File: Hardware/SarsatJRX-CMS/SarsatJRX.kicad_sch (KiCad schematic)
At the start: 37 parts, among them J3 LilyPi GPIO Header, U1 TLC2274, U2 TLC2274

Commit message: Added schematics.
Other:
- company: (none) -> F4JRX - ADRASEC 31
- title: (none) -> SarsatJRX signal board
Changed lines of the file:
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@@
 	(generator_version "9.0")
 	(paper "A4")
+	(title_block
+		(title "SarsatJRX signal board")
+		(date "2025-05-23")
+		(rev "v1.0")
+		(company "F4JRX - ADRASEC 31")
+		(comment 1 "Based on the work of Jean-Paul YONNET (F1LVT) : https://f1lvt.com/")
+		(comment 2 "SIgnal board for SarsatJRX decoder by F4JRX")
+	)
 	(junction
 		(at 262.89 43.18)

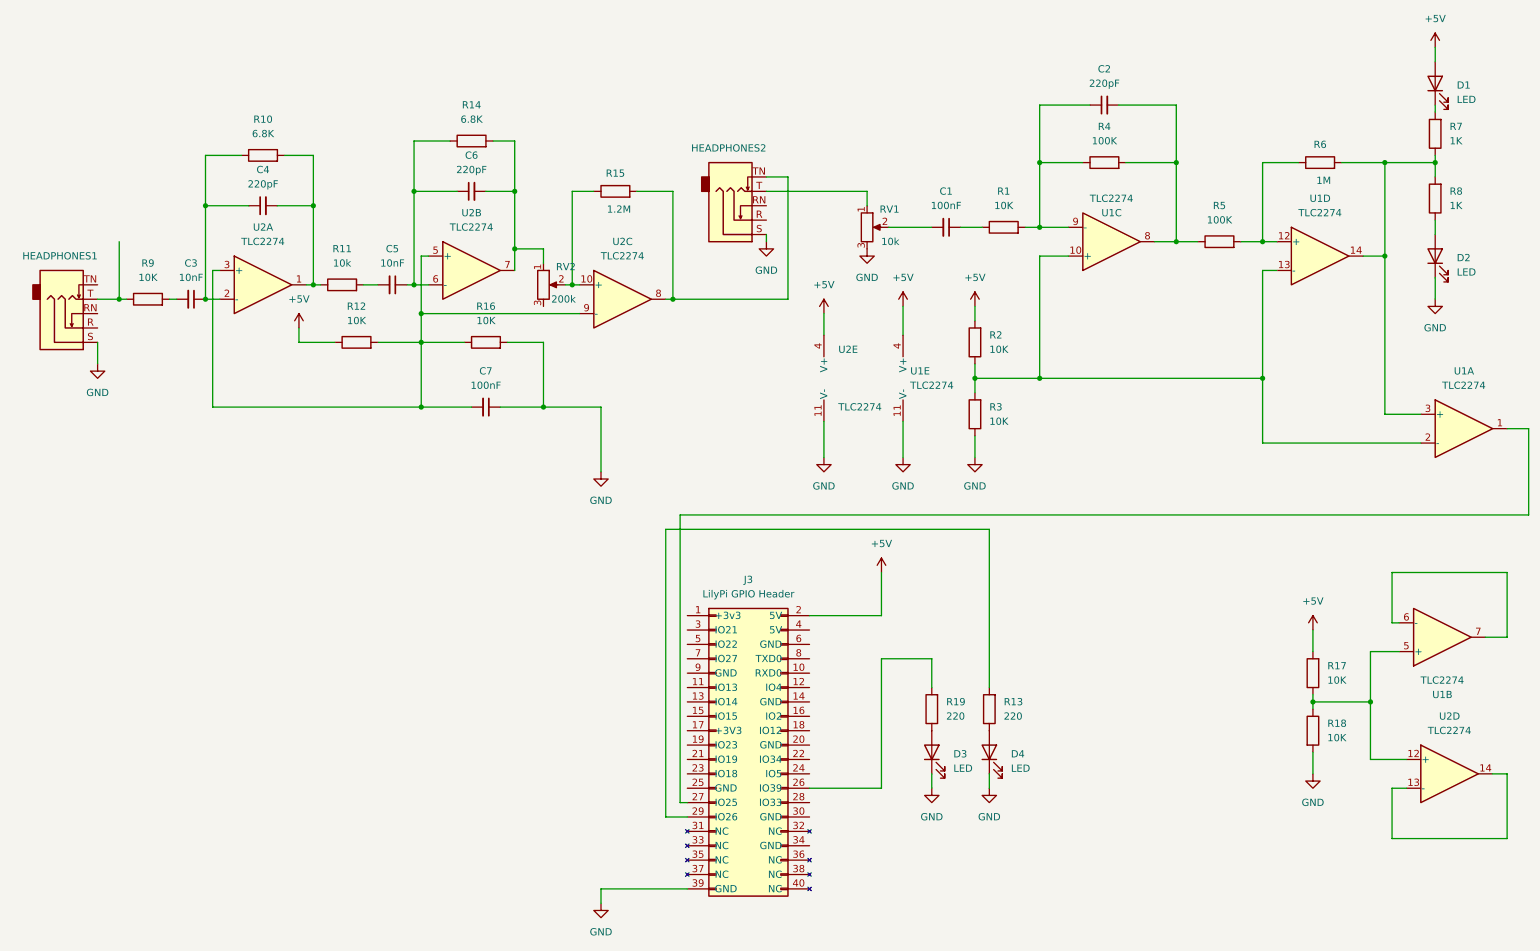
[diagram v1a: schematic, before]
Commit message: First step to v1.1 of the board : - Added buzzer on IO33 - Mouved led err to IO04 - Added voltage adaptation (5v->3.3v) on Receiver pin (IO25) - Added discri jack insertion detection on IO39 - Added audio input on IO34 - Added decoupling capacitors on 5V power supply for U1 and U2 to try and prevent spikes when wifi is activated - Added ground plane on bottom side of the PCB
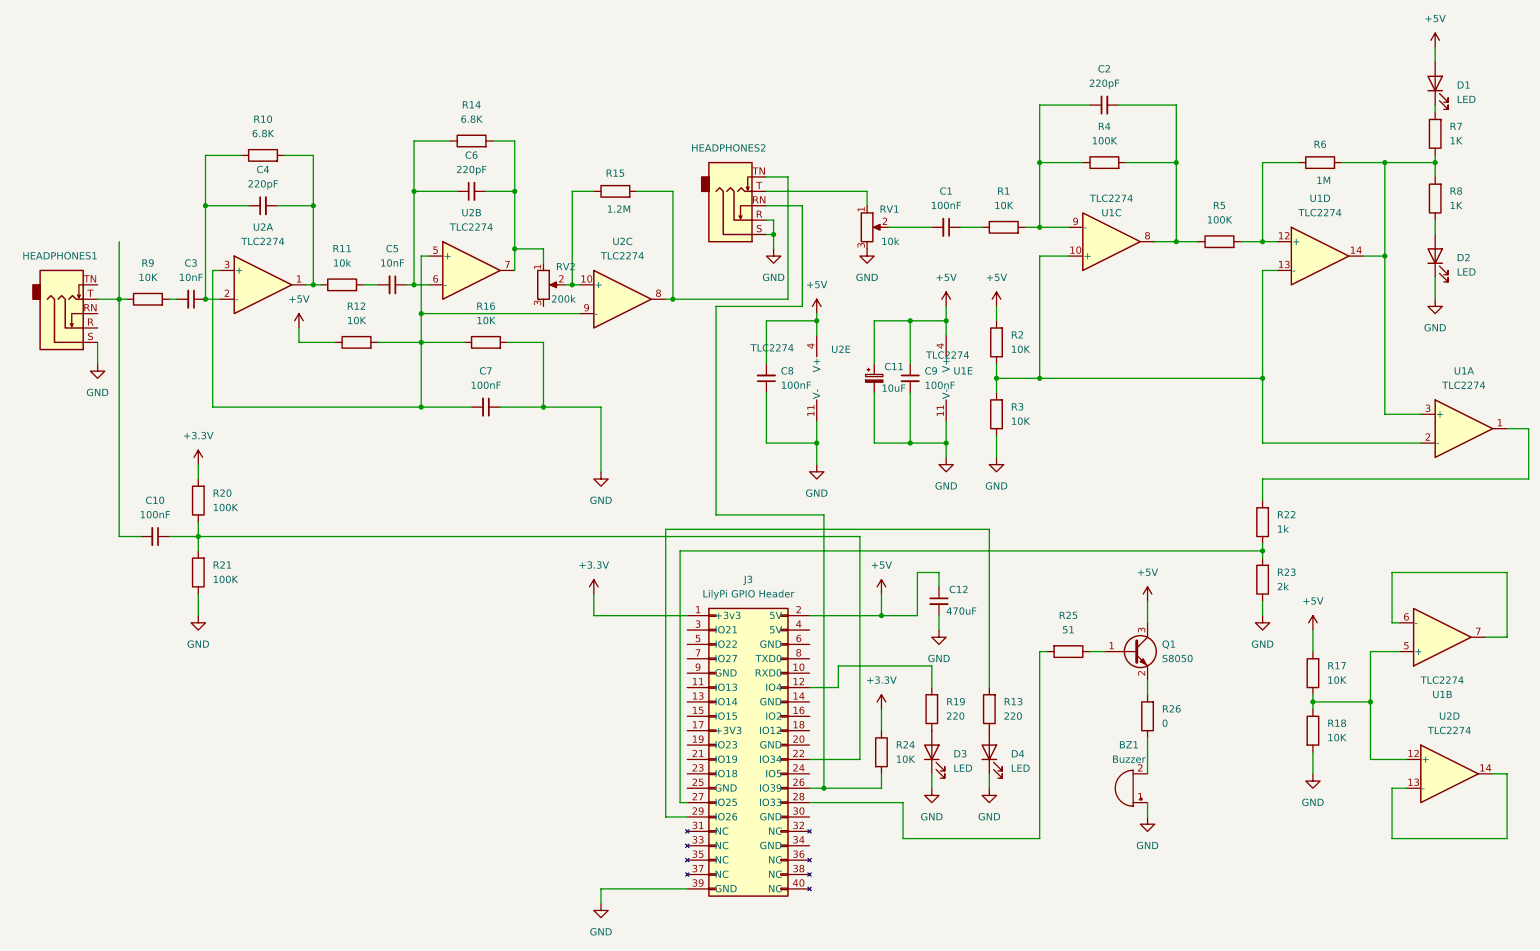
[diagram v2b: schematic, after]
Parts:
- added BZ1: Buzzer, Buzzer:MagneticBuzzer_PUI_AT-0927-TT-6-R-side-horn, symbol Device:Buzzer
- added C10, C8, C9: 100nF, Capacitor_SMD:C_0603_1608Metric, symbol Device:C_Small
- added C11: 10uF, Capacitor_Tantalum_SMD:CP_EIA-3216-18_Kemet-A, symbol Device:C_Polarized_Small
- added C12: 470uF, Capacitor_THT:CP_Radial_D8.0mm_P3.50mm, symbol Device:C_Small
- added Q1: S8050, j3y:SOT-23-3_L3.0-W1.7-P0.95-LS2.9-BR, symbol Transistor_BJT:S8050
- added R20, R21: 100K, Resistor_SMD:R_0603_1608Metric, symbol Device:R
- added R22: 1k, Resistor_SMD:R_0603_1608Metric, symbol Device:R
- added R23: 2k, Resistor_SMD:R_0603_1608Metric, symbol Device:R
- added R24: 10K, Resistor_SMD:R_0603_1608Metric, symbol Device:R
- added R25: 51, Resistor_SMD:R_0603_1608Metric, symbol Device:R
- added R26: 0, Resistor_SMD:R_0603_1608Metric, symbol Device:R
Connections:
- net +5V: now also C11.1, C12.1, C8.2, C9.1, Q1.3 (C)
- net GND: now also HEADPHONES2.R, BZ1.1 (+), C11.2, C12.2, C8.1, C9.2, R21.1, R23.1
- net +3.3V: now reaches J3.1 (+3v3)
- net +3.3V: now also R20.2, R24.1
- net at J3.12 (IO4): now also R19.2
- net at J3.22 (IO34): now also C10.1, R20.1, R21.2
- net at J3.26 (IO39): now also HEADPHONES2.RN, R24.2; no longer R19.2
- net at J3.27 (IO25): now also R22.1, R23.2; no longer U1.1
- net at J3.28 (IO33): now also R25.2
- net at HEADPHONES1.T, R9.1: now also C10.2
- new net: BZ1.2 (-), R26.1
- new net: Q1.2 (E), R26.2
- new net: Q1.1 (B), R25.1
- new net: R22.2, U1.1
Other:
- moved on the sheet: R2, R3, U1E, U2E

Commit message: Added test points.
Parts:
- added TP1, TP2, TP3, TP4, TP5, TP6: ~, TestPoint:TestPoint_Pad_D1.0mm, symbol Connector:TestPoint
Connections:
- net at C3.1, C4.1, R10.1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: now also TP6.1
- net at C10.2, HEADPHONES1.T, R9.1: now also TP3.1
- net at J3.27 (IO25), R22.1, R23.2: now also TP2.1
- net at R22.2, U1.1: now also TP1.1
- net at C2.1, R1.2, R4.1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: now also TP5.1
- net at HEADPHONES2.T, RV1.1: now also TP4.1

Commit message: Fixed more silk screen. Added 2 test points.
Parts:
- added TP7, TP8: ~, TestPoint:TestPoint_Pad_D1.0mm, symbol Connector:TestPoint
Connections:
- net at HEADPHONES2.RN, J3.26 (IO39), R24.2: now also TP8.1
- net at C10.1, J3.22 (IO34), R20.1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: now also TP7.1
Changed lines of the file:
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@@
 	)
 	(junction
+		(at 142.24 105.41)
+		(diameter 0)
+		(color 0 0 0 0)
+	)
+	(junction
 		(at 110.49 64.77)
 		(diameter 0)
@@
 	)
 	(junction
+		(at 78.74 109.22)
+		(diameter 0)
+		(color 0 0 0 0)
+	)
+	(junction
 		(at 232.41 111.76)
 		(diameter 0)
@@
 	(wire
 		(pts
-			(xy 44.45 109.22) (xy 161.29 109.22)
+			(xy 44.45 109.22) (xy 78.74 109.22)
 		)
 		(stroke
@@
 	(wire
 		(pts
+			(xy 78.74 109.22) (xy 161.29 109.22)
+		)
+		(stroke
+			(width 0)
+			(type default)
+		)
+	)
+	(wire
+		(pts
 			(xy 176.53 88.9) (xy 176.53 92.71)
 		)
@@
 	(wire
 		(pts
-			(xy 135.89 105.41) (xy 154.94 105.41)
+			(xy 135.89 105.41) (xy 142.24 105.41)
 		)
 		(stroke
@@
 	(wire
 		(pts
+			(xy 142.24 105.41) (xy 154.94 105.41)
+		)
+		(stroke
+			(width 0)
+			(type default)
+		)
+	)
+	(wire
+		(pts
 			(xy 163.83 71.12) (xy 170.18 71.12)
 		)
@@
 	)
 	(symbol
+		(lib_id "Connector:TestPoint")
+		(at 142.24 105.41 0)
+		(unit 1)
+		(exclude_from_sim no)
+		(in_bom yes)
+		(on_board yes)
+		(dnp no)
+		(property "Reference" "TP8"
+			(at 141.224 100.33 0)
+			(effects
+				(font
+					(size 1.27 1.27)
+				)
+				(justify left)
+			)
+		)
+		(property "Value" "~"
+			(at 144.78 103.378 0)
+			(effects
+				(font
+					(size 1.27 1.27)
+				)
+				(justify left)
+			)
+		)
+		(property "Footprint" "TestPoint:TestPoint_Pad_D1.0mm"
+			(at 147.32 105.41 0)
+			(effects
+				(font
+					(size 1.27 1.27)
+				)
+				(hide yes)
+			)
+		)
+		(property "Datasheet" "~"
+			(at 147.32 105.41 0)
+			(effects
+				(font
+					(size 1.27 1.27)
+				)
+				(hide yes)
+			)
+		)
+		(property "Description" "test point"
+			(at 142.24 105.41 0)
+			(effects
+				(font
+					(size 1.27 1.27)
+				)
+				(hide yes)
+			)
+		)
+		(pin "1"
+		)
+		(instances
+			(project "SarsatJRX"
+				(path "/756f9ab3-bcf2-4930-b1a2-703f1d715265"
+					(reference "TP8")
+					(unit 1)
+				)
+			)
+		)
+	)
+	(symbol
 		(lib_id "power:GND")
 		(at 184.15 153.67 0)
@@
 					(unit 1)
 				)
+			)
+		)
+	)
+	(symbol
+		(lib_id "Connector:TestPoint")
+		(at 78.74 109.22 0)
+		(unit 1)
+		(exclude_from_sim no)
+		(in_bom yes)
+		(on_board yes)
+		(dnp no)
+		(property "Reference" "TP7"
+			(at 77.724 104.14 0)
+			(effects
+				(font
+					(size 1.27 1.27)
+				)
+				(justify left)
+			)
+		)
+		(property "Value" "~"
+			(at 81.28 107.188 0)
+			(effects
+				(font
+					(size 1.27 1.27)
+				)
+				(justify left)
+			)
+		)
+		(property "Footprint" "TestPoint:TestPoint_Pad_D1.0mm"
+			(at 83.82 109.22 0)
+			(effects
+				(font
+					(size 1.27 1.27)
+				)
+				(hide yes)
+			)
+		)
+		(property "Datasheet" "~"
+			(at 83.82 109.22 0)
+			(effects
+				(font
+					(size 1.27 1.27)
+				)
+				(hide yes)
+			)
+		)
+		(property "Description" "test point"
+			(at 78.74 109.22 0)
+			(effects
+				(font
+					(size 1.27 1.27)
+				)
+				(hide yes)
+			)
+		)
+		(pin "1"
+		)
+		(instances
+			(project "SarsatJRX"
+				(path "/756f9ab3-bcf2-4930-b1a2-703f1d715265"
+					(reference "TP7")
+					(unit 1)
+				)

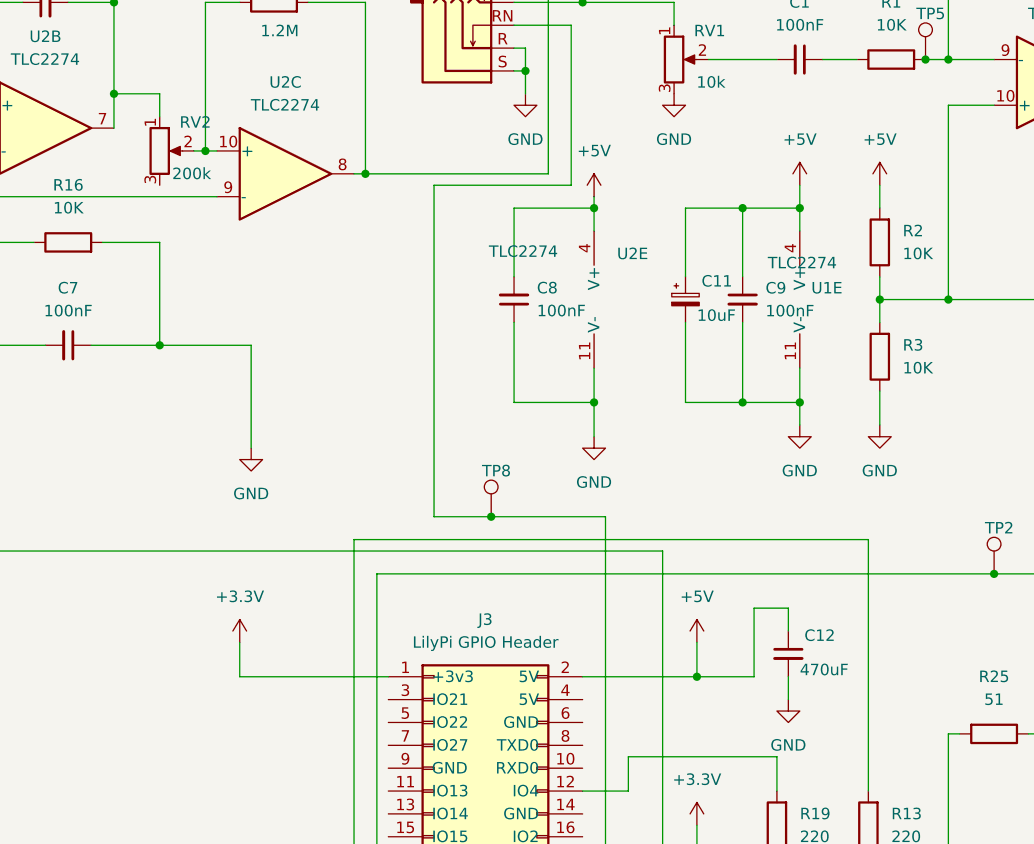
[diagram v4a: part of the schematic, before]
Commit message: Fixed 5V line capacitor value (3300uF) + footprint. Added decoupling capacitor to U2 power line. Added RV1/2 value sikl screen. Added slik screen to mark connector pins that have to be soldered. Moved to v1.2.
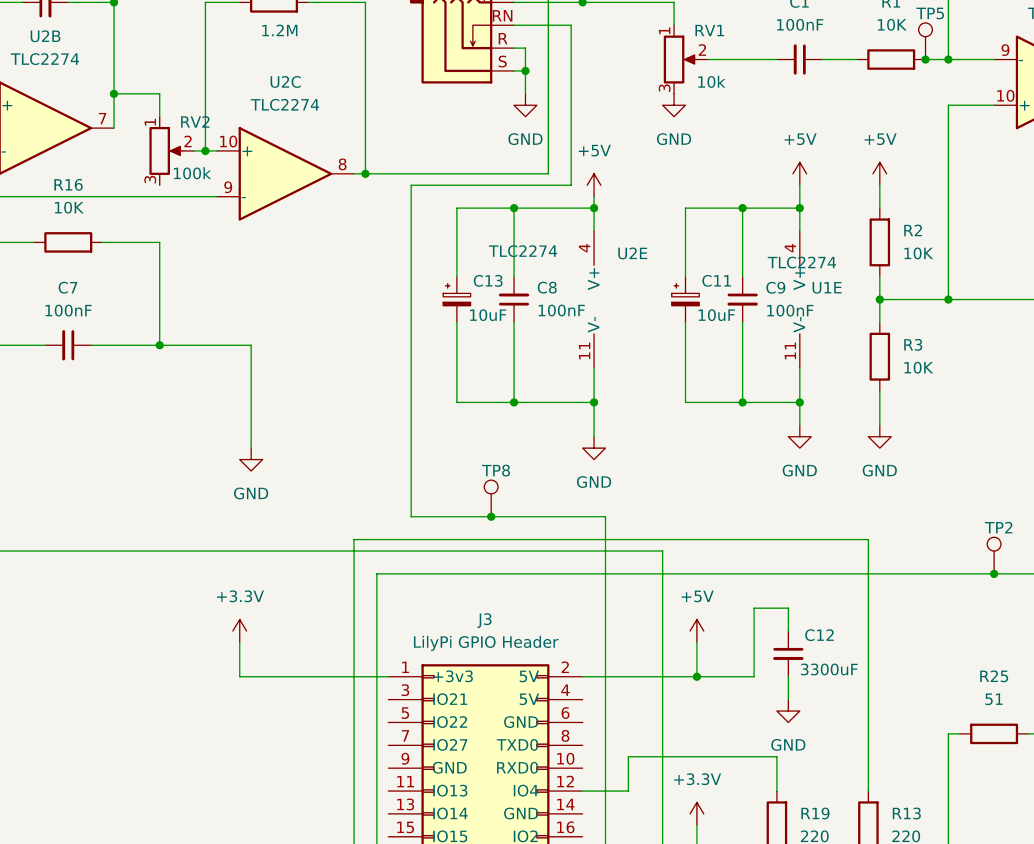
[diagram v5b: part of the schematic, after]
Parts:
- added C13: 10uF, Capacitor_Tantalum_SMD:CP_EIA-3216-18_Kemet-A, symbol Device:C_Polarized_Small
- C12: value 470uF -> 3300uF
- RV2: value 200k -> 100k
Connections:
- net +5V: now also C13.1
- net GND: now also C13.2
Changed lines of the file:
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@@
 	)
 	(junction
+		(at 144.78 71.12)
+		(diameter 0)
+		(color 0 0 0 0)
+	)
+	(junction
 		(at 128.27 67.31)
 		(diameter 0)
@@
 	)
 	(junction
+		(at 144.78 92.71)
+		(diameter 0)
+		(color 0 0 0 0)
+	)
+	(junction
 		(at 153.67 92.71)
 		(diameter 0)
@@
 	(wire
 		(pts
+			(xy 138.43 71.12) (xy 138.43 78.74)
+		)
+		(stroke
+			(width 0)
+			(type default)
+		)
+	)
+	(wire
+		(pts
 			(xy 175.26 123.19) (xy 175.26 125.73)
 		)
@@
 	(wire
 		(pts
-			(xy 151.13 68.58) (xy 135.89 68.58)
+			(xy 151.13 68.58) (xy 133.35 68.58)
 		)
 		(stroke
@@
 	(wire
 		(pts
+			(xy 144.78 71.12) (xy 138.43 71.12)
+		)
+		(stroke
+			(width 0)
+			(type default)
+		)
+	)
+	(wire
+		(pts
 			(xy 83.82 74.93) (xy 83.82 86.36)
 		)
@@
 	(wire
 		(pts
+			(xy 138.43 83.82) (xy 138.43 92.71)
+		)
+		(stroke
+			(width 0)
+			(type default)
+		)
+	)
+	(wire
+		(pts
 			(xy 128.27 67.31) (xy 148.59 67.31)
 		)
@@
 	(wire
 		(pts
-			(xy 135.89 68.58) (xy 135.89 105.41)
+			(xy 133.35 68.58) (xy 133.35 105.41)
 		)
 		(stroke
@@
 	(wire
 		(pts
-			(xy 135.89 105.41) (xy 142.24 105.41)
+			(xy 133.35 105.41) (xy 142.24 105.41)
 		)
 		(stroke
@@
 	(wire
 		(pts
+			(xy 138.43 92.71) (xy 144.78 92.71)
+		)
+		(stroke
+			(width 0)
+			(type default)
+		)
+	)
+	(wire
+		(pts
 			(xy 48.26 62.23) (xy 46.99 62.23)
 		)
@@
 	)
 	(symbol
+		(lib_id "Device:C_Polarized_Small")
+		(at 138.43 81.28 0)
+		(unit 1)
+		(exclude_from_sim no)
+		(in_bom yes)
+		(on_board yes)
+		(dnp no)
+		(property "Reference" "C13"
+			(at 140.208 79.248 0)
+			(effects
+				(font
+					(size 1.27 1.27)
+				)
+				(justify left)
+			)
+		)
+		(property "Value" "10uF"
+			(at 139.7 83.058 0)
+			(effects
+				(font
+					(size 1.27 1.27)
+				)
+				(justify left)
+			)
+		)
+		(property "Footprint" "Capacitor_Tantalum_SMD:CP_EIA-3216-18_Kemet-A"
+			(at 138.43 81.28 0)
+			(effects
+				(font
+					(size 1.27 1.27)
+				)
+				(hide yes)
+			)
+		)
+		(property "Datasheet" "~"
+			(at 138.43 81.28 0)
+			(effects
+				(font
+					(size 1.27 1.27)
+				)
+				(hide yes)
+			)
+		)
+		(property "Description" "Polarized capacitor, small symbol"
+			(at 138.43 81.28 0)
+			(effects
+				(font
+					(size 1.27 1.27)
+				)
+				(hide yes)
+			)
+		)
+		(pin "1"
+		)
+		(pin "2"
+		)
+		(instances
+			(project "SarsatJRX"
+				(path "/756f9ab3-bcf2-4930-b1a2-703f1d715265"
+					(reference "C13")
+					(unit 1)
+				)
+			)
+		)
+	)
+	(symbol
 		(lib_id "Device:C_Small")
 		(at 175.26 120.65 0)
@@
 			)
 		)
-		(property "Value" "470uF"
+		(property "Value" "3300uF"
 			(at 176.53 122.428 0)
 			(effects
@@
 			)
 		)
-		(property "Value" "200k"
+		(property "Value" "100k"
 			(at 111.125 67.31 0)
 			(effects
